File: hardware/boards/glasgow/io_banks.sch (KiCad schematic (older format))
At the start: 16 parts, among them J10 Conn_01x03, J4 Conn_01x02, J5 Conn_02x22_Odd_Even, U30 ICE40HX8K-BG121

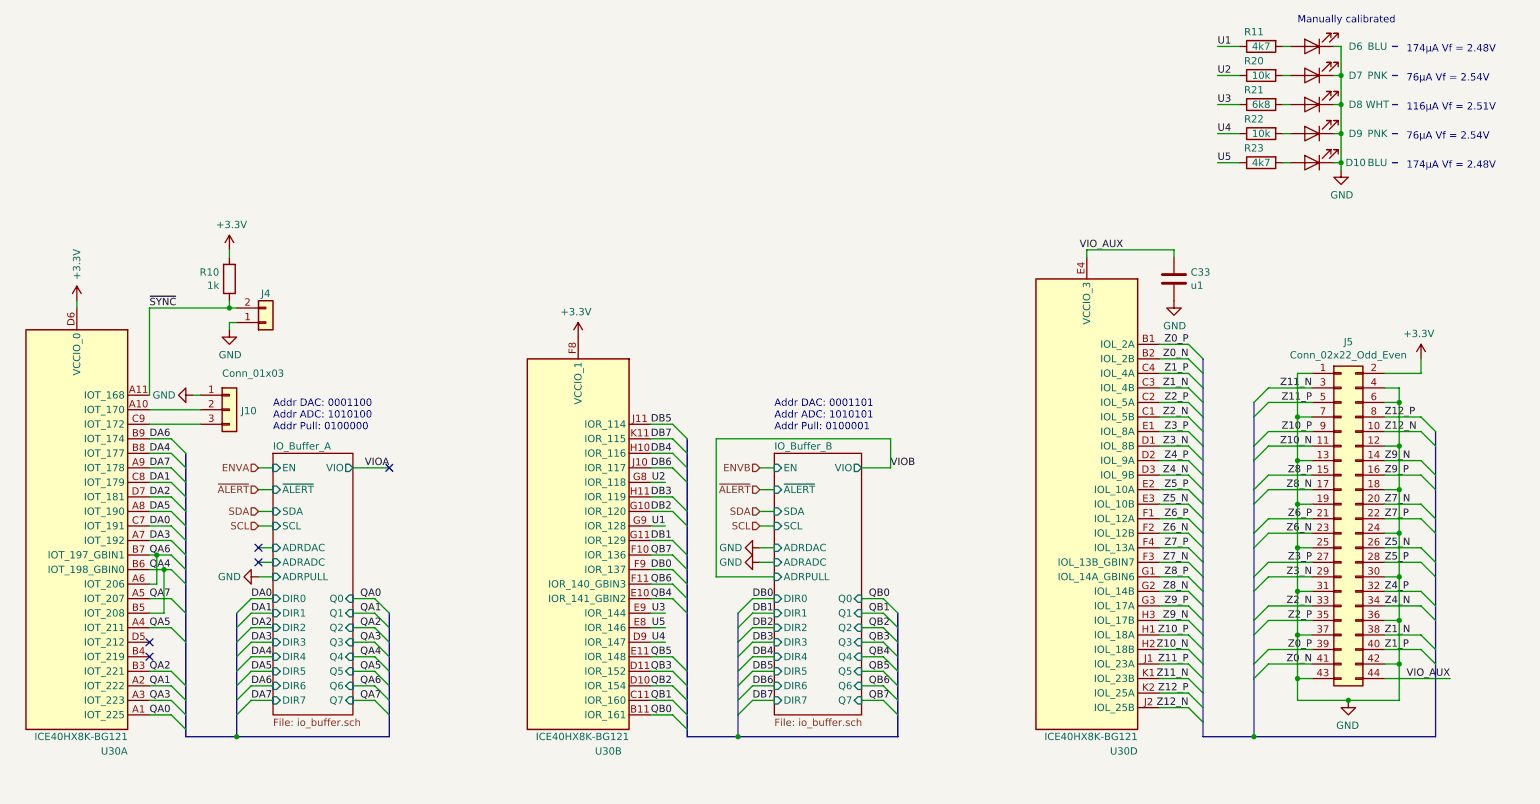
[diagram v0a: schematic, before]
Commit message: revC1: add level shifter to SYNC pin, using unused FPGA pin for DIR
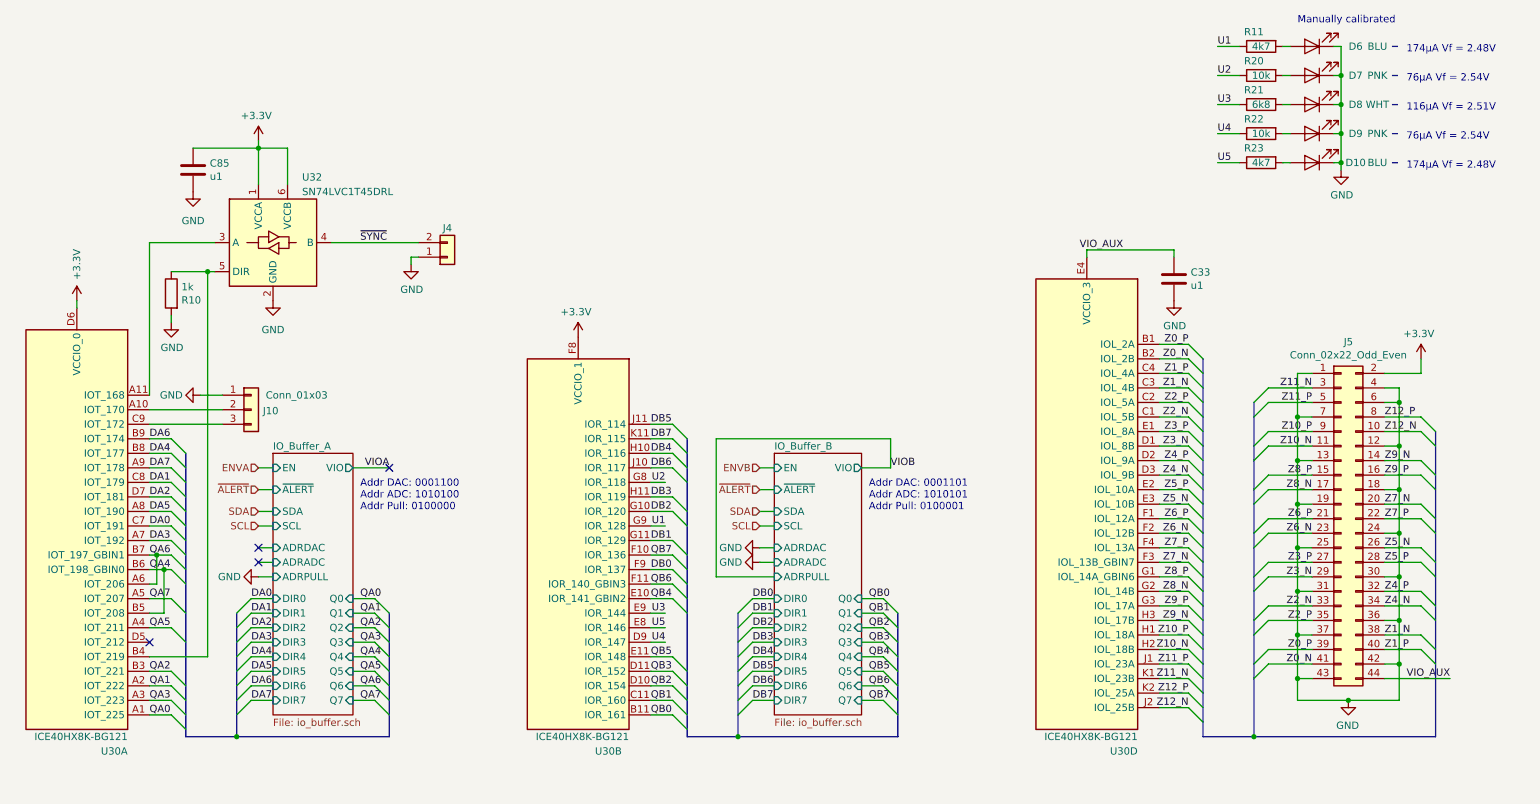
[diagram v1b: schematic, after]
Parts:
- added C85: u1, Capacitor_SMD:C_0402_1005Metric, symbol Device:C
- added U32: SN74LVC1T45DRL, Package_TO_SOT_SMD:SOT-563, symbol Logic_LevelTranslator:SN74LVC1T45DRL
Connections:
- net +3V3: now also C85.1, U32.1 (VCCA), U32.6 (VCCB); no longer R10.2
- net GND: now also R10.2, C85.2, U32.2 (GND)
- net ~SYNC: now also U32.4 (B); no longer R10.1, U30.A11 (IOT_168)
- net at U30.B4 (IOT_219): now also R10.1, U32.5 (DIR)
- new net: U30.A11 (IOT_168), U32.3 (A)
- no-connect marks 5 -> 4
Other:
- moved on the sheet: J10, J4, R10
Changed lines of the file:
@@
 	1    0    0    -1
 $EndComp
-Text Notes 2650 3700 0    50   ~ 0
+Text Notes 3250 4250 0    50   ~ 0
 Addr DAC: 0001100\nAddr ADC: 1010100\nAddr Pull: 0100000
 Wire Wire Line
@@
 	0    1    1    0
 $EndComp
-Text Notes 6100 3700 0    50   ~ 0
+Text Notes 6750 4250 0    50   ~ 0
 Addr DAC: 0001101\nAddr ADC: 1010101\nAddr Pull: 0100001
 Wire Wire Line
@@
 QA0
 NoConn ~ 1800 5150
-NoConn ~ 1800 5250
 Text Label 1800 4350 0    50   ~ 0
 DA0
@@
 L Connector_Generic:Conn_01x03 J10
 U 1 1 5C072C23
-P 2350 3550
-F 0 "J10" H 2430 3542 50  0000 L CNN
-F 1 "Conn_01x03" H 2300 3800 50  0000 L CNN
-F 2 "Connector_PinHeader_1.27mm:PinHeader_1x03_P1.27mm_Vertical" H 2350 3550 50  0001 C CNN
-F 3 "~" H 2350 3550 50  0001 C CNN
-	1    2350 3550
+P 2500 3550
+F 0 "J10" H 2580 3542 50  0000 L CNN
+F 1 "Conn_01x03" H 2600 3650 50  0000 L CNN
+F 2 "Connector_PinHeader_1.27mm:PinHeader_1x03_P1.27mm_Vertical" H 2500 3550 50  0001 C CNN
+F 3 "~" H 2500 3550 50  0001 C CNN
+	1    2500 3550
 	1    0    0    -1
 $EndComp
-Wire Wire Line
-	1800 3550 2150 3550
-Wire Wire Line
-	1800 3650 2150 3650
 $Comp
 L power:GND #PWR?
 U 1 1 5C0F528A
-P 2100 3450
+P 2150 3450
 AR Path="/5C0F528A" Ref="#PWR?"  Part="1"
 AR Path="/5C7B59B0/5C0F528A" Ref="#PWR0117"  Part="1"
-F 0 "#PWR0117" H 2100 3200 50  0001 C CNN
-F 1 "GND" V 2100 3250 50  0000 C CNN
-F 2 "" H 2100 3450 50  0001 C CNN
-F 3 "" H 2100 3450 50  0001 C CNN
-	1    2100 3450
+F 0 "#PWR0117" H 2150 3200 50  0001 C CNN
+F 1 "GND" V 2150 3250 50  0000 C CNN
+F 2 "" H 2150 3450 50  0001 C CNN
+F 3 "" H 2150 3450 50  0001 C CNN
+	1    2150 3450
 	0    1    1    0
 $EndComp
-Wire Wire Line
-	2100 3450 2150 3450
 $Comp
 L Connector_Generic:Conn_01x02 J?
 U 1 1 5C961091
-P 2600 2950
+P 3850 2500
 AR Path="/5C961091" Ref="J?"  Part="1"
 AR Path="/5C7B59B0/5C961091" Ref="J4"  Part="1"
-F 0 "J4" H 2600 2750 50  0000 C CNN
-F 1 "Conn_01x02" H 2680 2851 50  0001 L CNN
-F 2 "Connector_PinHeader_2.54mm:PinHeader_1x02_P2.54mm_Horizontal" H 2600 2950 50  0001 C CNN
-F 3 "https://www.mouser.hk/datasheet/2/418/NG_CD_640455_Y3-1255934.pdf" H 2600 2950 50  0001 C CNN
-F 4 "Molex" H -8000 100 50  0001 C CNN "Mfg"
-F 5 "22-05-3021" H -8000 100 50  0001 C CNN "MPN"
-	1    2600 2950
+F 0 "J4" H 3850 2300 50  0000 C CNN
+F 1 "Conn_01x02" H 3930 2401 50  0001 L CNN
+F 2 "Connector_PinHeader_2.54mm:PinHeader_1x02_P2.54mm_Horizontal" H 3850 2500 50  0001 C CNN
+F 3 "https://www.mouser.hk/datasheet/2/418/NG_CD_640455_Y3-1255934.pdf" H 3850 2500 50  0001 C CNN
+F 4 "Molex" H -6750 -350 50  0001 C CNN "Mfg"
+F 5 "22-05-3021" H -6750 -350 50  0001 C CNN "MPN"
+	1    3850 2500
 	1    0    0    1
 $EndComp
@@
 L power:GND #PWR?
 U 1 1 5C961098
-P 2350 3000
+P 3600 2550
 AR Path="/5C961098" Ref="#PWR?"  Part="1"
 AR Path="/5C7B59B0/5C961098" Ref="#PWR042"  Part="1"
-F 0 "#PWR042" H 2350 2750 50  0001 C CNN
-F 1 "GND" H 2355 2827 50  0000 C CNN
-F 2 "" H 2350 3000 50  0001 C CNN
-F 3 "" H 2350 3000 50  0001 C CNN
-	1    2350 3000
+F 0 "#PWR042" H 3600 2300 50  0001 C CNN
+F 1 "GND" H 3605 2377 50  0000 C CNN
+F 2 "" H 3600 2550 50  0001 C CNN
+F 3 "" H 3600 2550 50  0001 C CNN
+	1    3600 2550
 	1    0    0    -1
 $EndComp
 Wire Wire Line
-	2400 2950 2350 2950
-Wire Wire Line
-	2350 2950 2350 3000
-Text Label 1800 2850 0    50   ~ 0
+	3650 2500 3600 2500
+Wire Wire Line
+	3600 2500 3600 2550
+Text Label 3250 2400 0    50   ~ 0
 ~SYNC
 $Comp
 L Device:R R?
 U 1 1 5C9610A4
-P 2350 2650
+P 1950 2750
 AR Path="/5C9610A4" Ref="R?"  Part="1"
 AR Path="/5C7B59B0/5C9610A4" Ref="R10"  Part="1"
-F 0 "R10" H 2280 2604 50  0000 R CNN
-F 1 "1k" H 2280 2695 50  0000 R CNN
-F 2 "Resistor_SMD:R_0402_1005Metric" V 2280 2650 50  0001 C CNN
-F 3 "https://www.mouser.com/datasheet/2/447/PYu-AC_51_RoHS_L_6-1152827.pdf" H 2350 2650 50  0001 C CNN
-F 4 "Yageo" H -8000 100 50  0001 C CNN "Mfg"
-F 5 "AC0603FR-07130RL" H -8000 100 50  0001 C CNN "MPN"
-	1    2350 2650
-	1    0    0    1
-$EndComp
-$Comp
-L power:+3.3V #PWR?
-U 1 1 5C9610AB
-P 2350 2450
-AR Path="/5C9610AB" Ref="#PWR?"  Part="1"
-AR Path="/5C7B59B0/5C9610AB" Ref="#PWR041"  Part="1"
-F 0 "#PWR041" H 2350 2300 50  0001 C CNN
-F 1 "+3.3V" H 2365 2623 50  0000 C CNN
-F 2 "" H 2350 2450 50  0001 C CNN
-F 3 "" H 2350 2450 50  0001 C CNN
-	1    2350 2450
-	1    0    0    -1
-$EndComp
-Wire Wire Line
-	2350 2450 2350 2500
-Wire Wire Line
-	2350 2800 2350 2850
-Connection ~ 2350 2850
-Wire Wire Line
-	2350 2850 2400 2850
-Wire Wire Line
-	1800 2850 1800 3450
-Wire Wire Line
-	1800 2850 2350 2850
+F 0 "R10" H 1880 2704 50  0000 R CNN
+F 1 "1k" H 1880 2795 50  0000 R CNN
+F 2 "Resistor_SMD:R_0402_1005Metric" V 1880 2750 50  0001 C CNN
+F 3 "https://www.mouser.com/datasheet/2/447/PYu-AC_51_RoHS_L_6-1152827.pdf" H 1950 2750 50  0001 C CNN
+F 4 "Yageo" H -8400 200 50  0001 C CNN "Mfg"
+F 5 "AC0603FR-07130RL" H -8400 200 50  0001 C CNN "MPN"
+	1    1950 2750
+	-1   0    0    -1
+$EndComp
 $Comp
 L FPGA_Lattice:ICE40HX8K-BG121 U?
@@
 Wire Wire Line
 	9150 1050 9300 1050
+$Comp
+L Logic_LevelTranslator:SN74LVC1T45DRL U32
+U 1 1 5CA4F297
+P 2650 2400
+F 0 "U32" H 2850 2850 50  0000 L CNN
+F 1 "SN74LVC1T45DRL" H 2850 2750 50  0000 L CNN
+F 2 "Package_TO_SOT_SMD:SOT-563" H 2650 1950 50  0001 C CNN
+F 3 "http://www.ti.com/lit/ds/symlink/sn74lvc1t45.pdf" H 1750 1750 50  0001 C CNN
+	1    2650 2400
+	1    0    0    -1
+$EndComp
+Wire Wire Line
+	3050 2400 3650 2400
+Wire Wire Line
+	1800 3550 2300 3550
+Wire Wire Line
+	1800 3650 2300 3650
+Wire Wire Line
+	2150 3450 2300 3450
+Wire Wire Line
+	2250 2600 2200 2600
+$Comp
+L power:GND #PWR?
+U 1 1 5CBEC27E
+P 2650 2800
+AR Path="/5CBEC27E" Ref="#PWR?"  Part="1"
+AR Path="/5C7B59B0/5CBEC27E" Ref="#PWR0130"  Part="1"
+F 0 "#PWR0130" H 2650 2550 50  0001 C CNN
+F 1 "GND" H 2650 2600 50  0000 C CNN
+F 2 "" H 2650 2800 50  0001 C CNN
+F 3 "" H 2650 2800 50  0001 C CNN
+	1    2650 2800
+	1    0    0    -1
+$EndComp
+$Comp
+L power:+3.3V #PWR?
+U 1 1 5CBEC3EE
+P 2550 1700
+AR Path="/5CBEC3EE" Ref="#PWR?"  Part="1"
+AR Path="/5C7B59B0/5CBEC3EE" Ref="#PWR0129"  Part="1"
+F 0 "#PWR0129" H 2550 1550 50  0001 C CNN
+F 1 "+3.3V" H 2565 1873 50  0000 C CNN
+F 2 "" H 2550 1700 50  0001 C CNN
+F 3 "" H 2550 1700 50  0001 C CNN
+	1    2550 1700
+	-1   0    0    -1
+$EndComp
+$Comp
+L power:GND #PWR?
+U 1 1 5CC04643
+P 1950 2950
+AR Path="/5CC04643" Ref="#PWR?"  Part="1"
+AR Path="/5C7B59B0/5CC04643" Ref="#PWR0127"  Part="1"
+F 0 "#PWR0127" H 1950 2700 50  0001 C CNN
+F 1 "GND" H 1955 2777 50  0000 C CNN
+F 2 "" H 1950 2950 50  0001 C CNN
+F 3 "" H 1950 2950 50  0001 C CNN
+	1    1950 2950
+	1    0    0    -1
+$EndComp
+Wire Wire Line
+	1800 2400 2250 2400
+Wire Wire Line
+	1800 2400 1800 3450
+Wire Wire Line
+	1950 2600 2200 2600
+Wire Wire Line
+	1800 5250 2200 5250
+Connection ~ 2200 2600
+Wire Wire Line
+	1950 2900 1950 2950
+Wire Wire Line
+	2200 2600 2200 5250
+$Comp
+L Device:C C?
+U 1 1 5CCC4D9E
+P 2100 1900
+AR Path="/5CCC4D9E" Ref="C?"  Part="1"
+AR Path="/5C7B59B0/5CCC4D9E" Ref="C85"  Part="1"
+F 0 "C85" H 2215 1946 50  0000 L CNN
+F 1 "u1" H 2215 1855 50  0000 L CNN
+F 2 "Capacitor_SMD:C_0402_1005Metric" H 2138 1750 50  0001 C CNN
+F 3 "https://www.mouser.hk/datasheet/2/396/mlcc02_e-1307760.pdf" H 2100 1900 50  0001 C CNN
+F 4 "Taiyo Yuden" H -4550 500 50  0001 C CNN "Mfg"
+F 5 "TMK107BJ154KA-T" H -4550 500 50  0001 C CNN "MPN"
+	1    2100 1900
+	1    0    0    -1
+$EndComp
+$Comp
+L power:GND #PWR?
+U 1 1 5CCC4E88
+P 2100 2050
+AR Path="/5CCC4E88" Ref="#PWR?"  Part="1"
+AR Path="/5C7B59B0/5CCC4E88" Ref="#PWR0128"  Part="1"
+F 0 "#PWR0128" H 2100 1800 50  0001 C CNN
+F 1 "GND" H 2100 1850 50  0000 C CNN
+F 2 "" H 2100 2050 50  0001 C CNN
+F 3 "" H 2100 2050 50  0001 C CNN
+	1    2100 2050
+	1    0    0    -1
+$EndComp
+Wire Wire Line
+	2100 1750 2550 1750
+Wire Wire Line
+	2550 1750 2550 2000
+Connection ~ 2550 1750
+Wire Wire Line
+	2750 1750 2750 2000
+Wire Wire Line
+	2550 1750 2550 1700
+Wire Wire Line
+	2550 1750 2750 1750
 Wire Bus Line
-	5850 4950 5850 5800
+	2400 4950 2400 5800
+Wire Bus Line
+	3450 4950 3450 5800
 Wire Bus Line
 	6950 4950 6950 5800
 Wire Bus Line
-	3450 4950 3450 5800
-Wire Bus Line
-	2400 4950 2400 5800
+	5850 4950 5850 5800
 Wire Bus Line
 	10650 3700 10650 5800
@@
 	9400 3500 9400 5800
 Wire Bus Line
+	2050 3850 2050 5800
+Wire Bus Line
 	5500 3750 5500 5800
 Wire Bus Line
-	2050 3850 2050 5800
-Wire Bus Line
 	9050 3200 9050 5800

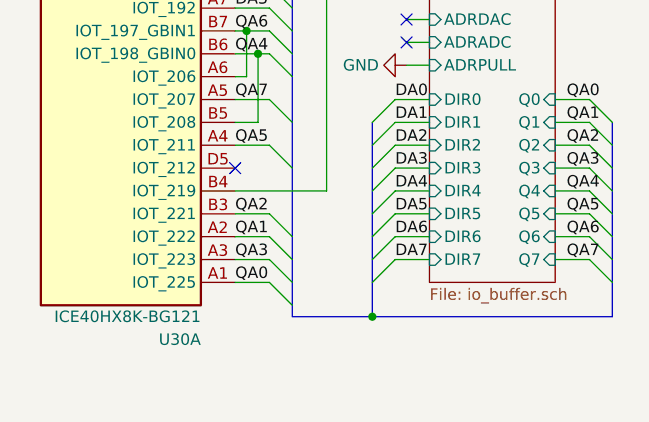
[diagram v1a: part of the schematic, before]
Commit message: revC1: route FPGA pin D5 to CLKREF
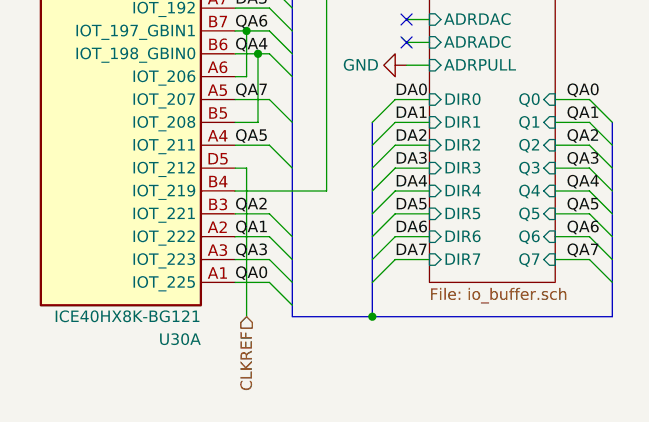
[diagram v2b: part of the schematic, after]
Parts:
- U32: footprint Package_TO_SOT_SMD:SOT-563 -> Glasgow:SOT-563
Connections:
- net CLKREF: now reaches U30.D5 (IOT_212)
- no-connect marks 4 -> 3
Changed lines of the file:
@@
 Text Label 1800 5650 0    50   ~ 0
 QA0
-NoConn ~ 1800 5150
 Text Label 1800 4350 0    50   ~ 0
 DA0
@@
 F 0 "U32" H 2850 2850 50  0000 L CNN
 F 1 "SN74LVC1T45DRL" H 2850 2750 50  0000 L CNN
-F 2 "Package_TO_SOT_SMD:SOT-563" H 2650 1950 50  0001 C CNN
+F 2 "Glasgow:SOT-563" H 2650 1950 50  0001 C CNN
 F 3 "http://www.ti.com/lit/ds/symlink/sn74lvc1t45.pdf" H 1750 1750 50  0001 C CNN
 	1    2650 2400
@@
 Wire Wire Line
 	2550 1750 2750 1750
+Text HLabel 1850 5800 3    50   Input ~ 0
+CLKREF
+Wire Wire Line
+	1800 5150 1850 5150
+Wire Wire Line
+	1850 5150 1850 5800
 Wire Bus Line
 	2400 4950 2400 5800

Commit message: revC1: change AUX pin header .05" -> .1"
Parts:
- J10: footprint Connector_PinHeader_1.27mm:PinHeader_1x03_P1.27mm_Vertical -> Connector_PinHeader_2.54mm:PinHeader_1x03_P2.54mm_Vertical
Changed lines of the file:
@@
 F 0 "J10" H 2580 3542 50  0000 L CNN
 F 1 "Conn_01x03" H 2600 3650 50  0000 L CNN
-F 2 "Connector_PinHeader_1.27mm:PinHeader_1x03_P1.27mm_Vertical" H 2500 3550 50  0001 C CNN
+F 2 "Connector_PinHeader_2.54mm:PinHeader_1x03_P2.54mm_Vertical" H 2500 3550 50  0001 C CNN
 F 3 "~" H 2500 3550 50  0001 C CNN
 	1    2500 3550

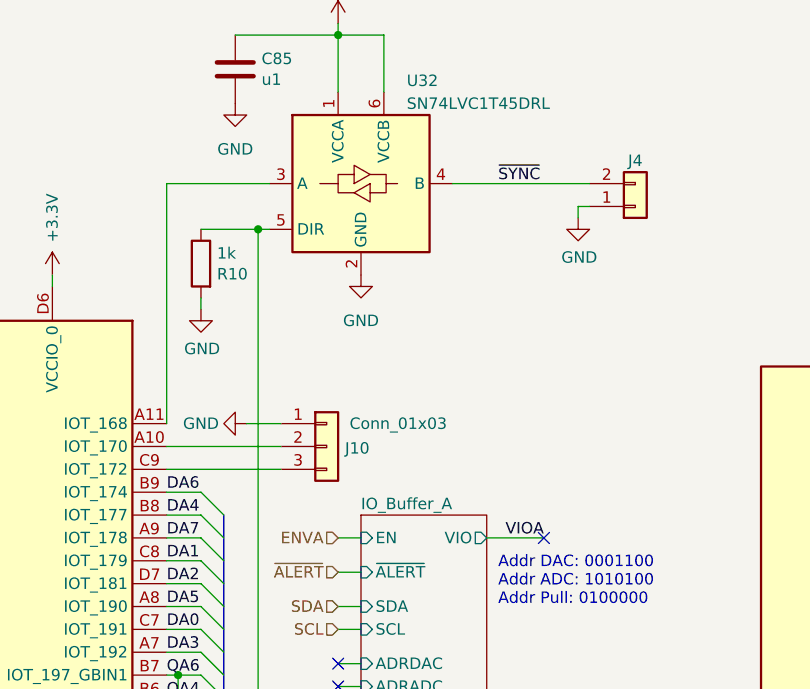
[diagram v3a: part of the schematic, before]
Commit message: revC1: add inline resistors to AUX/SYNC, add testpoints to rear
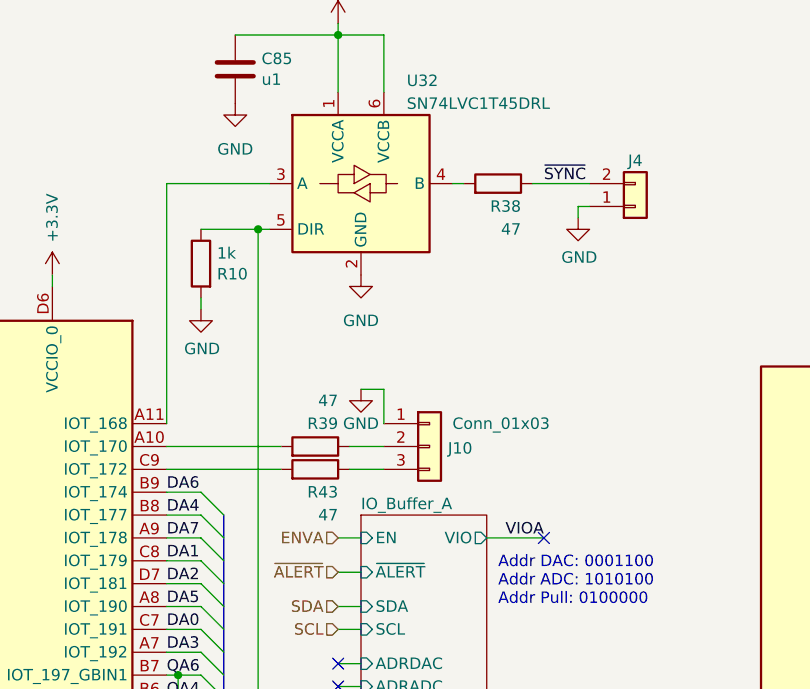
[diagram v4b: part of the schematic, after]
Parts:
- added R38, R39, R43: 47, Resistor_SMD:R_0402_1005Metric, symbol Device:R
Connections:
- net ~SYNC: now also R38.1; no longer U32.4 (B)
- net at J10.2 (Pin_2): now also R39.1; no longer U30.A10 (IOT_170)
- net at J10.3 (Pin_3): now also R43.1; no longer U30.C9 (IOT_172)
- new net: R39.2, U30.A10 (IOT_170)
- new net: R43.2, U30.C9 (IOT_172)
- new net: R38.2, U32.4 (B)
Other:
- moved on the sheet: J10
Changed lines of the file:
@@
 L Connector_Generic:Conn_01x03 J10
 U 1 1 5C072C23
-P 2500 3550
-F 0 "J10" H 2580 3542 50  0000 L CNN
-F 1 "Conn_01x03" H 2600 3650 50  0000 L CNN
-F 2 "Connector_PinHeader_2.54mm:PinHeader_1x03_P2.54mm_Vertical" H 2500 3550 50  0001 C CNN
-F 3 "~" H 2500 3550 50  0001 C CNN
-	1    2500 3550
+P 2950 3550
+F 0 "J10" H 3030 3542 50  0000 L CNN
+F 1 "Conn_01x03" H 3050 3650 50  0000 L CNN
+F 2 "Connector_PinHeader_2.54mm:PinHeader_1x03_P2.54mm_Vertical" H 2950 3550 50  0001 C CNN
+F 3 "~" H 2950 3550 50  0001 C CNN
+	1    2950 3550
 	1    0    0    -1
 $EndComp
@@
 L power:GND #PWR?
 U 1 1 5C0F528A
-P 2150 3450
+P 2650 3300
 AR Path="/5C0F528A" Ref="#PWR?"  Part="1"
 AR Path="/5C7B59B0/5C0F528A" Ref="#PWR0117"  Part="1"
-F 0 "#PWR0117" H 2150 3200 50  0001 C CNN
-F 1 "GND" V 2150 3250 50  0000 C CNN
-F 2 "" H 2150 3450 50  0001 C CNN
-F 3 "" H 2150 3450 50  0001 C CNN
-	1    2150 3450
-	0    1    1    0
+F 0 "#PWR0117" H 2650 3050 50  0001 C CNN
+F 1 "GND" H 2650 3150 50  0000 C CNN
+F 2 "" H 2650 3300 50  0001 C CNN
+F 3 "" H 2650 3300 50  0001 C CNN
+	1    2650 3300
+	1    0    0    -1
 $EndComp
 $Comp
@@
 Wire Wire Line
 	3600 2500 3600 2550
-Text Label 3250 2400 0    50   ~ 0
+Text Label 3450 2400 0    50   ~ 0
 ~SYNC
 $Comp
@@
 $EndComp
 Wire Wire Line
-	3050 2400 3650 2400
+	3050 2400 3100 2400
 Wire Wire Line
 	1800 3550 2300 3550
 Wire Wire Line
 	1800 3650 2300 3650
-Wire Wire Line
-	2150 3450 2300 3450
 Wire Wire Line
 	2250 2600 2200 2600
@@
 Wire Wire Line
 	1850 5150 1850 5800
+$Comp
+L Device:R R?
+U 1 1 5CBF4EC8
+P 3250 2400
+AR Path="/5CBF4EC8" Ref="R?"  Part="1"
+AR Path="/5C7B59B0/5CBF4EC8" Ref="R38"  Part="1"
+F 0 "R38" V 3150 2500 50  0000 R CNN
+F 1 "47" V 3050 2500 50  0000 R CNN
+F 2 "Resistor_SMD:R_0402_1005Metric" V 3180 2400 50  0001 C CNN
+F 3 "https://www.mouser.com/datasheet/2/447/PYu-AC_51_RoHS_L_6-1152827.pdf" H 3250 2400 50  0001 C CNN
+F 4 "Yageo" H -7100 -150 50  0001 C CNN "Mfg"
+F 5 "AC0603FR-07130RL" H -7100 -150 50  0001 C CNN "MPN"
+	1    3250 2400
+	0    1    -1   0
+$EndComp
+Wire Wire Line
+	3400 2400 3650 2400
+$Comp
+L Device:R R?
+U 1 1 5CBF658E
+P 2450 3550
+AR Path="/5CBF658E" Ref="R?"  Part="1"
+AR Path="/5C7B59B0/5CBF658E" Ref="R39"  Part="1"
+F 0 "R39" V 2550 3650 50  0000 R CNN
+F 1 "47" V 2650 3650 50  0000 R CNN
+F 2 "Resistor_SMD:R_0402_1005Metric" V 2380 3550 50  0001 C CNN
+F 3 "https://www.mouser.com/datasheet/2/447/PYu-AC_51_RoHS_L_6-1152827.pdf" H 2450 3550 50  0001 C CNN
+F 4 "Yageo" H -7900 1000 50  0001 C CNN "Mfg"
+F 5 "AC0603FR-07130RL" H -7900 1000 50  0001 C CNN "MPN"
+	1    2450 3550
+	0    1    -1   0
+$EndComp
+$Comp
+L Device:R R?
+U 1 1 5CBF65F8
+P 2450 3650
+AR Path="/5CBF65F8" Ref="R?"  Part="1"
+AR Path="/5C7B59B0/5CBF65F8" Ref="R43"  Part="1"
+F 0 "R43" V 2350 3750 50  0000 R CNN
+F 1 "47" V 2250 3750 50  0000 R CNN
+F 2 "Resistor_SMD:R_0402_1005Metric" V 2380 3650 50  0001 C CNN
+F 3 "https://www.mouser.com/datasheet/2/447/PYu-AC_51_RoHS_L_6-1152827.pdf" H 2450 3650 50  0001 C CNN
+F 4 "Yageo" H -7900 1100 50  0001 C CNN "Mfg"
+F 5 "AC0603FR-07130RL" H -7900 1100 50  0001 C CNN "MPN"
+	1    2450 3650
+	0    1    -1   0
+$EndComp
+Wire Wire Line
+	2600 3650 2750 3650
+Wire Wire Line
+	2600 3550 2750 3550
+Wire Wire Line
+	2650 3300 2750 3300
+Wire Wire Line
+	2750 3300 2750 3450
 Wire Bus Line
 	2400 4950 2400 5800
